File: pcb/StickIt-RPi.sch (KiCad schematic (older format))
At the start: 30 parts, among them CON1 BARREL_JACK, J1 JSHORTNORMAL, J3 XuLA_IO_HDR, J4 JSHORTNORMAL, J5 JSHORTNORMAL, SW1 SW_PUSH, U1 NCV1117, U2 EEPROM_I2C

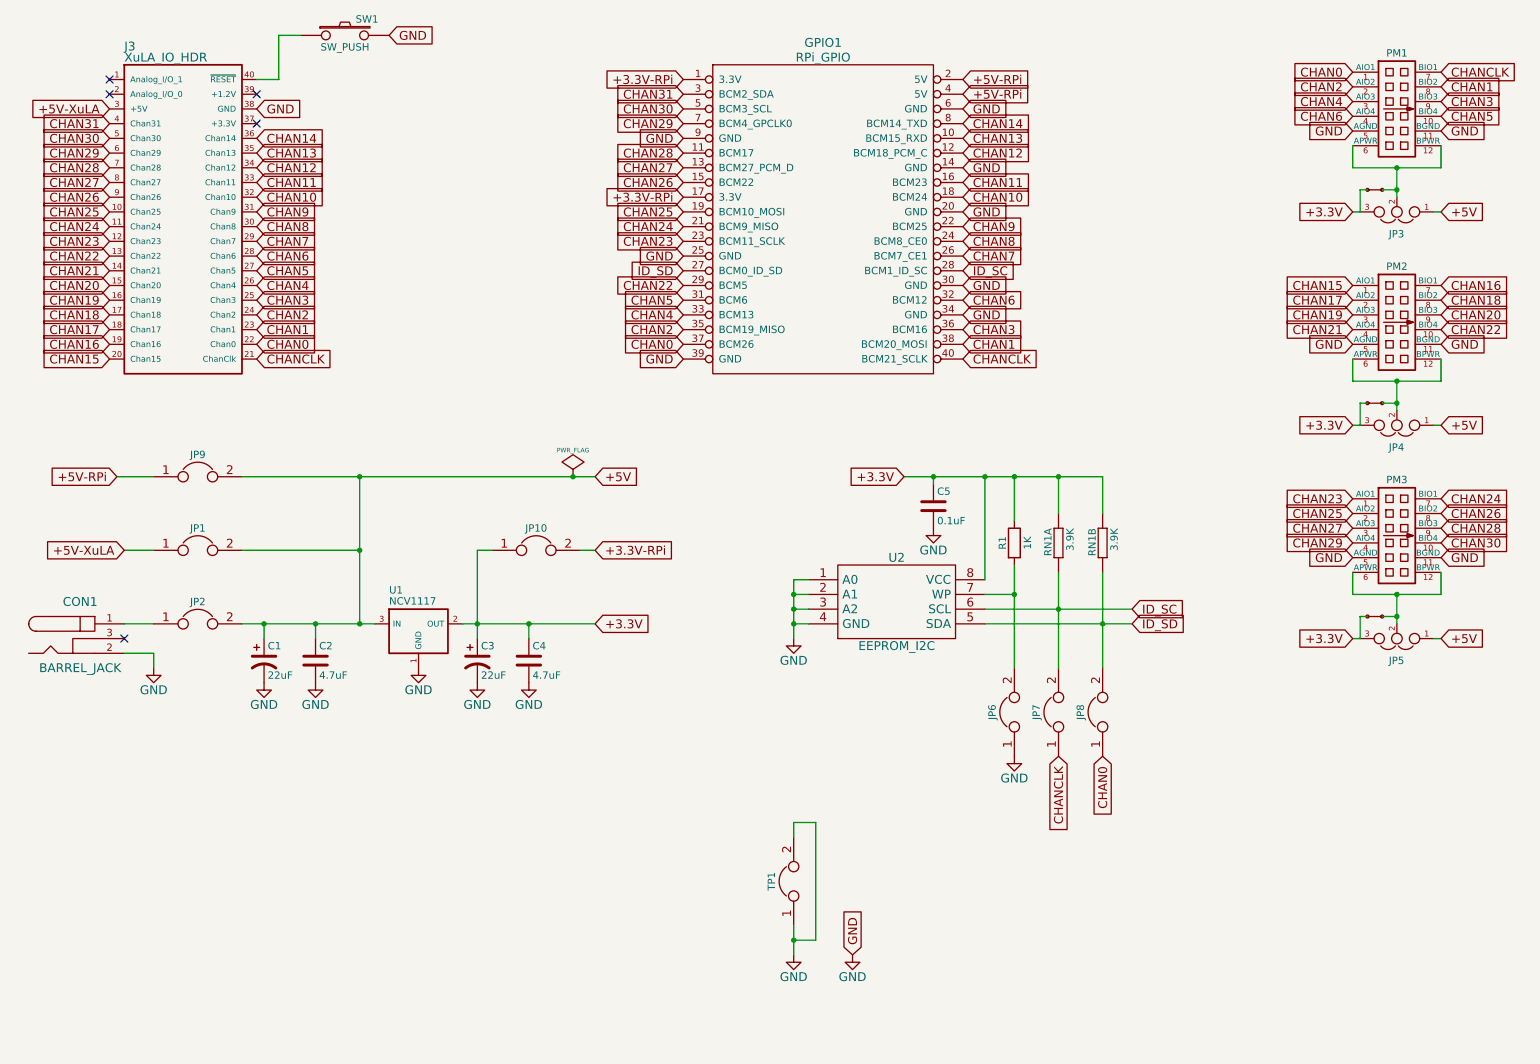
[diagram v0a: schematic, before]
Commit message: Updated component reference identifiers.
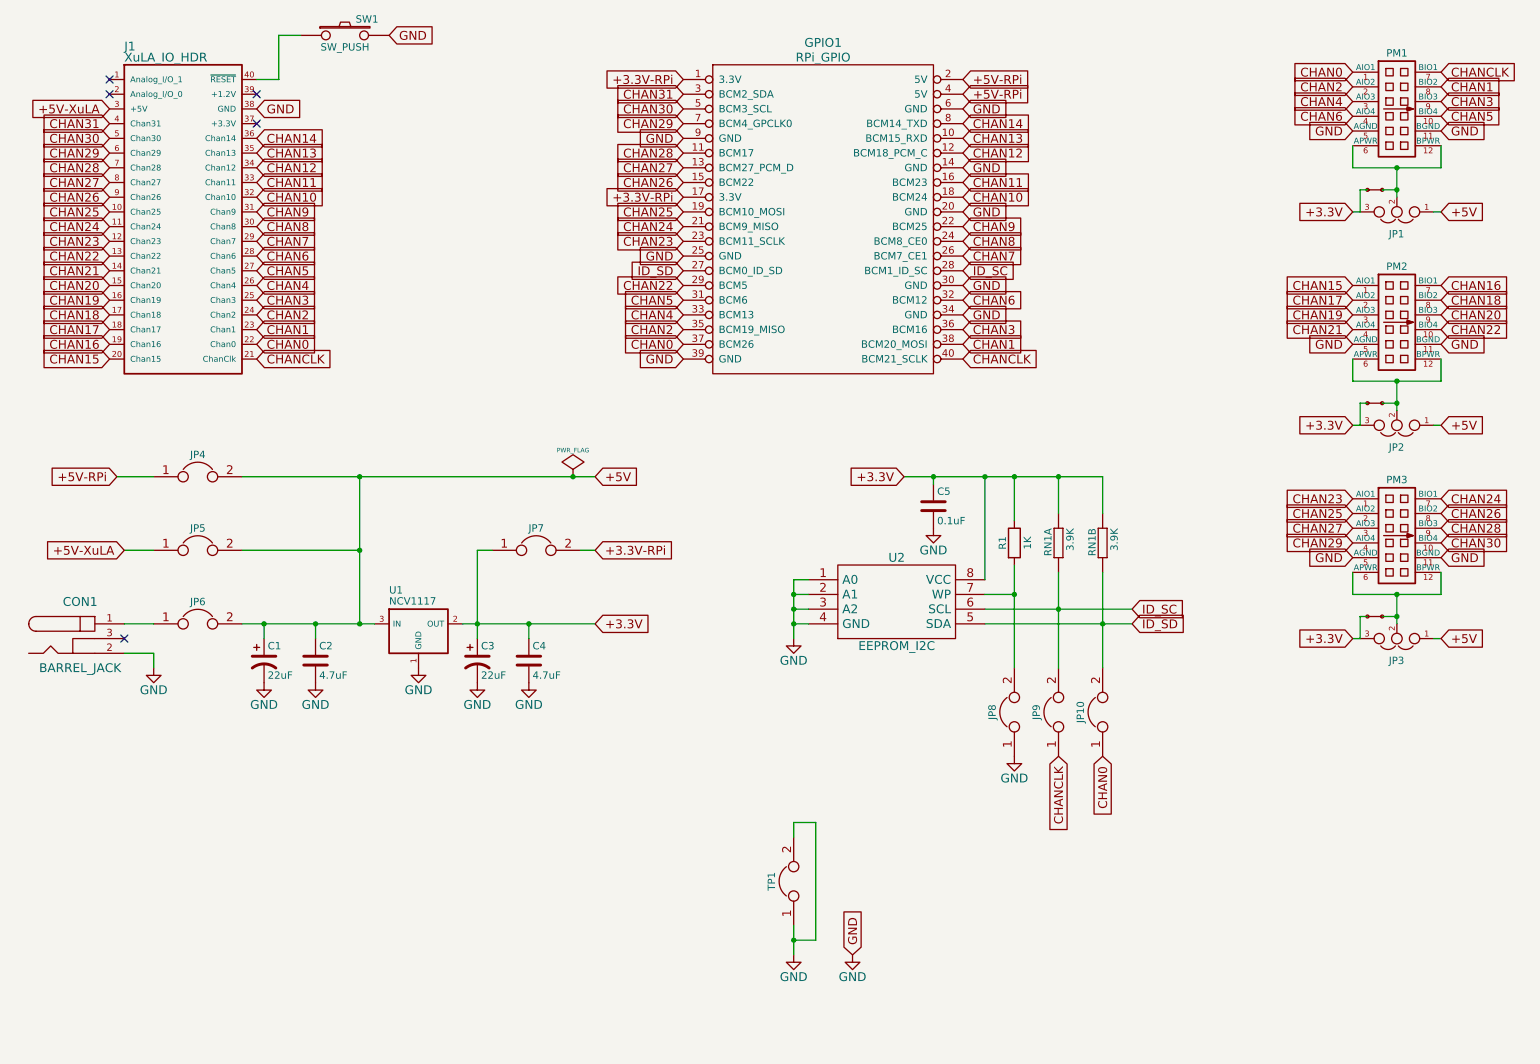
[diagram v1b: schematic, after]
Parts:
- renumbered J3 to J1, J1 to J3, JP3 to JP1, JP8 to JP10, JP4 to JP2, JP5 to JP3, JP9 to JP4, JP1 to JP5, JP2 to JP6, JP10 to JP7, JP6 to JP8, JP7 to JP9
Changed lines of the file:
@@
 +5V
 $Comp
-L XuLA_IO_HDR J3
+L XuLA_IO_HDR J1
 U 1 1 55181E79
 P 1250 1050
-F 0 "J3" H 1350 1275 60  0000 L CNN
+F 0 "J1" H 1350 1275 60  0000 L CNN
 F 1 "XuLA_IO_HDR" H 1350 1200 60  0000 L CNN
 F 2 "XESS:XuLA_IO_Hdr" H 1250 1050 60  0001 C CNN
@@
 GND
 $Comp
-L JUMPER3 JP3
+L JUMPER3 JP1
 U 1 1 55182078
 P 10000 1950
-F 0 "JP3" H 9950 2100 50  0000 L CNN
+F 0 "JP1" H 9950 2100 50  0000 L CNN
 F 1 "JUMPER3" H 10000 2050 50  0001 C BNN
 F 2 "XESS:HDR_1x3" H 10000 1950 60  0001 C CNN
@@
 	2400 750  2550 750
 $Comp
-L JSHORTNORMAL J1
+L JSHORTNORMAL J3
 U 1 1 55181943
 P 9900 1800
-F 0 "J1" H 9900 1700 50  0001 L BNN
+F 0 "J3" H 9900 1700 50  0001 L BNN
 F 1 "JSHORTNORMAL" H 9800 1700 50  0001 L BNN
 F 2 "XESS:xess-JSHORT" H 9900 1950 50  0001 C CNN
@@
 $EndComp
 $Comp
-L JUMPER JP1
+L JUMPER JP5
 U 1 1 55182A6A
 P 1850 4250
-F 0 "JP1" H 1850 4400 50  0000 C CNN
+F 0 "JP5" H 1850 4400 50  0000 C CNN
 F 1 "JUMPER" H 1850 4170 50  0001 C CNN
 F 2 "XESS:HDR_1x2" H 1850 4250 60  0001 C CNN
@@
 $EndComp
 $Comp
-L JUMPER JP2
+L JUMPER JP6
 U 1 1 55182B35
 P 1850 4750
-F 0 "JP2" H 1850 4900 50  0000 C CNN
+F 0 "JP6" H 1850 4900 50  0000 C CNN
 F 1 "JUMPER" H 1850 4670 50  0001 C CNN
 F 2 "XESS:HDR_1x2" H 1850 4750 60  0001 C CNN
@@
 GND
 $Comp
-L JUMPER3 JP5
+L JUMPER3 JP3
 U 1 1 5518392B
 P 10000 4850
-F 0 "JP5" H 9950 5000 50  0000 L CNN
+F 0 "JP3" H 9950 5000 50  0000 L CNN
 F 1 "JUMPER3" H 10000 4950 50  0001 C BNN
 F 2 "XESS:HDR_1x3" H 10000 4850 60  0001 C CNN
@@
 GND
 $Comp
-L JUMPER3 JP4
+L JUMPER3 JP2
 U 1 1 55183A1E
 P 10000 3400
-F 0 "JP4" H 9950 3550 50  0000 L CNN
+F 0 "JP2" H 9950 3550 50  0000 L CNN
 F 1 "JUMPER3" H 10000 3500 50  0001 C BNN
 F 2 "XESS:HDR_1x3" H 10000 3400 60  0001 C CNN
@@
 +3.3V
 $Comp
-L JUMPER JP6
+L JUMPER JP8
 U 1 1 551AEBDC
 P 7400 5350
-F 0 "JP6" H 7400 5500 50  0000 C CNN
+F 0 "JP8" H 7400 5500 50  0000 C CNN
 F 1 "JUMPER" H 7400 5270 50  0001 C CNN
 F 2 "XESS:HDR_1x2" H 7400 5350 60  0001 C CNN
@@
 $EndComp
 $Comp
-L JUMPER JP7
+L JUMPER JP9
 U 1 1 551AECE7
 P 7700 5350
-F 0 "JP7" H 7700 5500 50  0000 C CNN
+F 0 "JP9" H 7700 5500 50  0000 C CNN
 F 1 "JUMPER" H 7700 5270 50  0001 C CNN
 F 2 "XESS:HDR_1x2" H 7700 5350 60  0001 C CNN
@@
 $EndComp
 $Comp
-L JUMPER JP8
+L JUMPER JP10
 U 1 1 551AED33
 P 8000 5350
-F 0 "JP8" H 8000 5500 50  0000 C CNN
+F 0 "JP10" H 8000 5500 50  0000 C CNN
 F 1 "JUMPER" H 8000 5270 50  0001 C CNN
 F 2 "XESS:HDR_1x2" H 8000 5350 60  0001 C CNN
@@
 +5V-RPi
 $Comp
-L JUMPER JP9
+L JUMPER JP4
 U 1 1 551B8C71
 P 1850 3750
-F 0 "JP9" H 1850 3900 50  0000 C CNN
+F 0 "JP4" H 1850 3900 50  0000 C CNN
 F 1 "JUMPER" H 1850 3670 50  0001 C CNN
 F 2 "XESS:HDR_1x2" H 1850 3750 60  0001 C CNN
@@
 +3.3V-RPi
 $Comp
-L JUMPER JP10
+L JUMPER JP7
 U 1 1 551C21A9
 P 4150 4250
-F 0 "JP10" H 4150 4400 50  0000 C CNN
+F 0 "JP7" H 4150 4400 50  0000 C CNN
 F 1 "JUMPER" H 4150 4170 50  0001 C CNN
 F 2 "XESS:HDR_1x2" H 4150 4250 60  0001 C CNN

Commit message: Added Grove connectors.
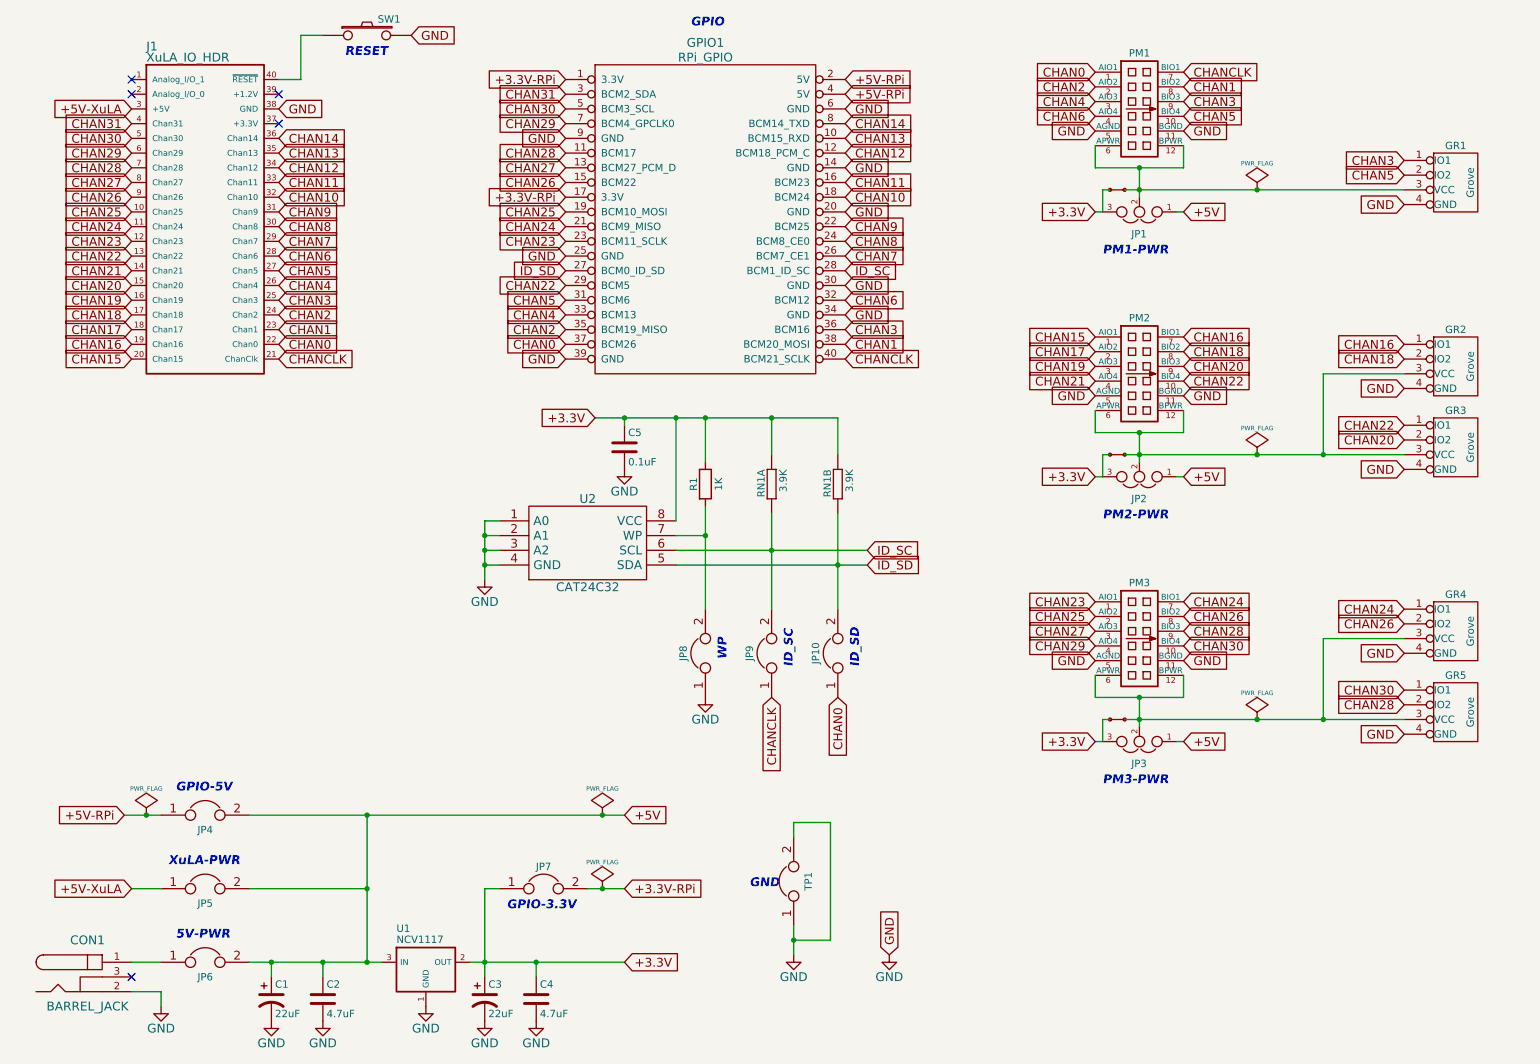
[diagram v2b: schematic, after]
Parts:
- added GR1, GR2, GR3, GR4, GR5: Grove, XESS:GROVE_MALE, symbol Grove_Male
- U2: value EEPROM_I2C -> CAT24C32
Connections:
- net CHAN16: now also GR2.1 (IO1)
- net CHAN18: now also GR2.2 (IO2)
- net CHAN20: now also GR3.2 (IO2)
- net CHAN22: now also GR3.1 (IO1)
- net CHAN24: now also GR4.1 (IO1)
- net CHAN26: now also GR4.2 (IO2)
- net CHAN28: now also GR5.2 (IO2)
- net CHAN3: now also GR1.1 (IO1)
- net CHAN30: now also GR5.1 (IO1)
- net CHAN5: now also GR1.2 (IO2)
- net GND: now also GR1.4 (GND), GR2.4 (GND), GR3.4 (GND), GR4.4 (GND), GR5.4 (GND)
- net at J3.1, JP1.2, PM1.12 (BPWR)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: now also GR1.3 (VCC)
- net at J5.1, JP3.2, PM3.12 (BPWR)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: now also GR4.3 (VCC), GR5.3 (VCC)
- net at J4.1, JP2.2, PM2.12 (BPWR)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: now also GR2.3 (VCC), GR3.3 (VCC)
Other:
- note added: "5V-PWR"
- note added: "GND"
- note added: "GPIO"
- note added: "GPIO-3.3V"
- note added: "GPIO-5V"
- note added: "ID_SC"
- note added: "ID_SD"
- note added: "PM1-PWR"
- note added: "PM2-PWR"
- note added: "PM3-PWR"
- note added: "RESET"
- note added: "WP"
- note added: "XuLA-PWR"
- moved on the sheet: C1, C2, C3, C4, C5, CON1, GPIO1, J1, JP1, JP10, JP2, JP3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

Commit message: Changed PCB footprints for reset switch, capacitors and resistor.
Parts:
- C1, C3: footprint Capacitors_SMD:c_elec_4x5.7 -> Capacitors_SMD:c_elec_5x5.3
- C2, C4: footprint Capacitors_SMD:C_0805 -> Resistors_SMD:R_0805_HandSoldering
- C5: footprint Capacitors_SMD:C_0603 -> Resistors_SMD:R_0805_HandSoldering
- R1: footprint Resistors_SMD:R_0603 -> Resistors_SMD:R_0805_HandSoldering
- SW1: footprint XESS:SW_EVP-AA002 -> XESS:RS-282G05A3-SM_RT
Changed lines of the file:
@@
 Sheet 1 1
 Title "StickIt! Motherboard / Raspberry Pi B+ Hat"
-Date "Friday, April 03, 2015"
-Rev "4.0"
+Date "Wednesday, May 06, 2015"
+Rev "4.1"
 Comp "XESS Corp."
 Comment1 "(c) 2015"
@@
 F 0 "SW1" H 3150 860 50  0000 C CNN
 F 1 "SW_PUSH" H 3000 670 50  0001 C CNN
-F 2 "XESS:SW_EVP-AA002" H 3000 750 60  0001 C CNN
+F 2 "XESS:RS-282G05A3-SM_RT" H 3000 750 60  0001 C CNN
 F 3 "" H 3000 750 60  0000 C CNN
 	1    3000 750
@@
 F 0 "C2" H 2725 7400 50  0000 L CNN
 F 1 "4.7uF" H 2725 7200 50  0000 L CNN
-F 2 "Capacitors_SMD:C_0805" H 2738 7150 30  0001 C CNN
+F 2 "Resistors_SMD:R_0805_HandSoldering" H 2738 7150 30  0001 C CNN
 F 3 "" H 2700 7300 60  0000 C CNN
 	1    2700 7300
@@
 F 0 "C1" H 2375 7400 50  0000 L CNN
 F 1 "22uF" H 2375 7200 50  0000 L CNN
-F 2 "Capacitors_SMD:c_elec_4x5.7" H 2350 7300 60  0001 C CNN
+F 2 "Capacitors_SMD:c_elec_5x5.3" H 2350 7300 60  0001 C CNN
 F 3 "" H 2350 7300 60  0000 C CNN
 	1    2350 7300
@@
 F 0 "C4" H 4175 7400 50  0000 L CNN
 F 1 "4.7uF" H 4175 7200 50  0000 L CNN
-F 2 "Capacitors_SMD:C_0805" H 4188 7150 30  0001 C CNN
+F 2 "Resistors_SMD:R_0805_HandSoldering" H 4188 7150 30  0001 C CNN
 F 3 "" H 4150 7300 60  0000 C CNN
 	1    4150 7300
@@
 F 0 "C3" H 3825 7400 50  0000 L CNN
 F 1 "22uF" H 3825 7200 50  0000 L CNN
-F 2 "Capacitors_SMD:c_elec_4x5.7" H 3800 7300 60  0001 C CNN
+F 2 "Capacitors_SMD:c_elec_5x5.3" H 3800 7300 60  0001 C CNN
 F 3 "" H 3800 7300 60  0000 C CNN
 	1    3800 7300
@@
 F 0 "R1" V 5220 3800 50  0000 C CNN
 F 1 "1K" V 5390 3800 50  0000 C CNN
-F 2 "Resistors_SMD:R_0603" V 5230 3800 30  0001 C CNN
+F 2 "Resistors_SMD:R_0805_HandSoldering" V 5230 3800 30  0001 C CNN
 F 3 "" H 5300 3800 30  0000 C CNN
 	1    5300 3800
@@
 F 0 "C5" H 4775 3650 50  0000 L CNN
 F 1 "0.1uF" H 4775 3450 50  0000 L CNN
-F 2 "Capacitors_SMD:C_0603" H 4788 3400 30  0001 C CNN
+F 2 "Resistors_SMD:R_0805_HandSoldering" H 4788 3400 30  0001 C CNN
 F 3 "" H 4750 3550 60  0000 C CNN
 	1    4750 3550
@@
 1E 25 49 2A DA F6 C4 5C B7 0C C3 B9 A4 0A 98 09 FC 0D B0 92 CD 57 CD 1F 06 4E 04 26 A7 75 27 49
 52 39 26 13 73 DE C3 6C BE 70 B5 12 F8 16 86 73 8D C3 FF 03 63 F8 EE 2E BE 9A 04 B1 00 00 00 00
-49 45 4E 44 AE 42 60 82 8F
+49 45 4E 44 AE 42 60 82 0F
 EndData
 $EndBitmap

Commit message: Removed two Grove connectors and rotated the others.
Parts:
- removed GR3, GR5: Grove, XESS:GROVE_MALE, symbol Grove_Male
- renumbered GR4 to GR3
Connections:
- net CHAN1: now also GR1.2 (IO2)
- net CHAN3: no longer GR1.1 (IO1)
- net CHAN5: no longer GR1.2 (IO2)
- net CHANCLK: now also GR1.1 (IO1)
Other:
- moved on the sheet: GR2, GR3
